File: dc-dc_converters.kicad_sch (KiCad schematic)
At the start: 62 parts, among them J3 JST_SH_1x4_SM04B-SRSS-TB-LF-SN, J4 Molex_Nano-Fit_1x2_105313-220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, U2 SIC477ED-T1-GE3, U3 AP62301WU-7, U4 AP62301WU-7

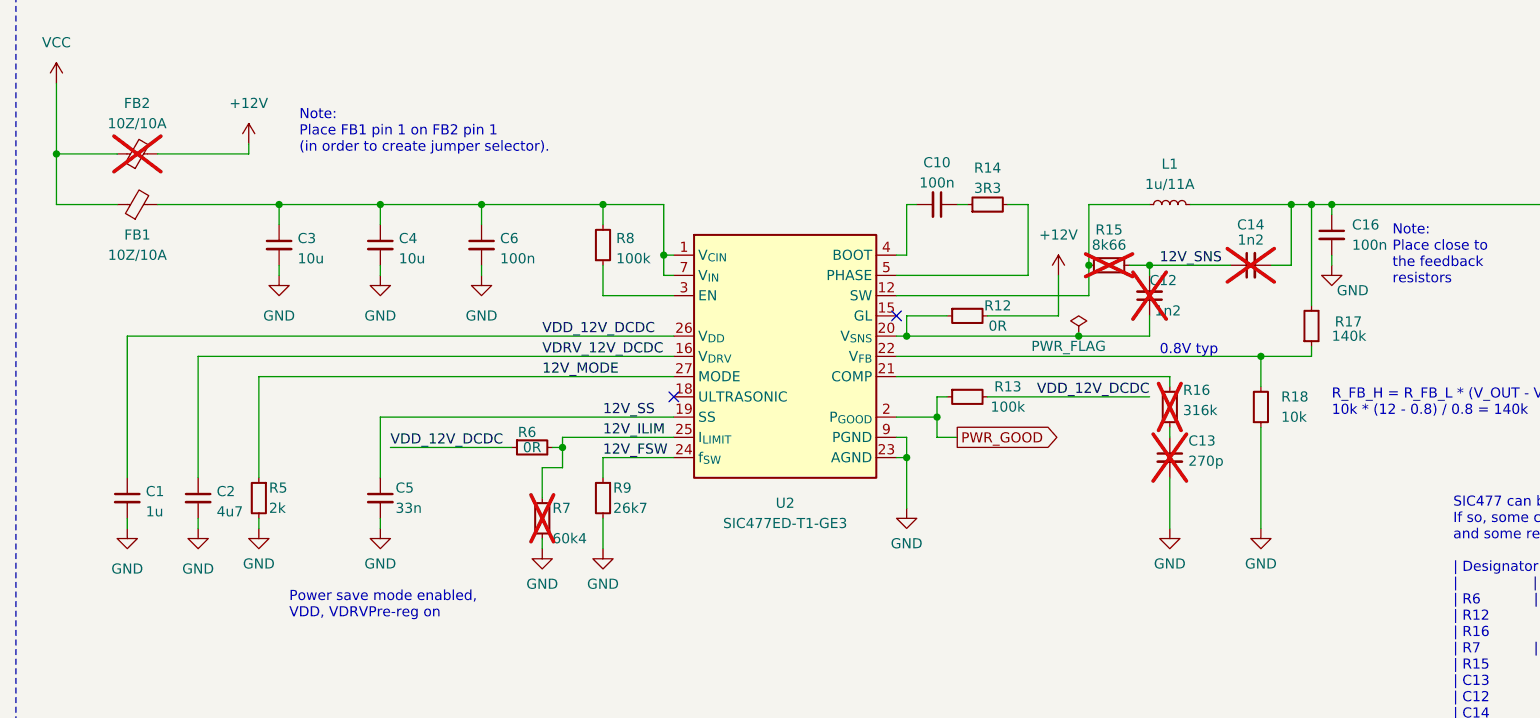
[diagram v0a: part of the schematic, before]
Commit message: [#57006] Change capacitors to higher voltage ratings
Homogenize capacitors (to not use multiple versions of the same params)
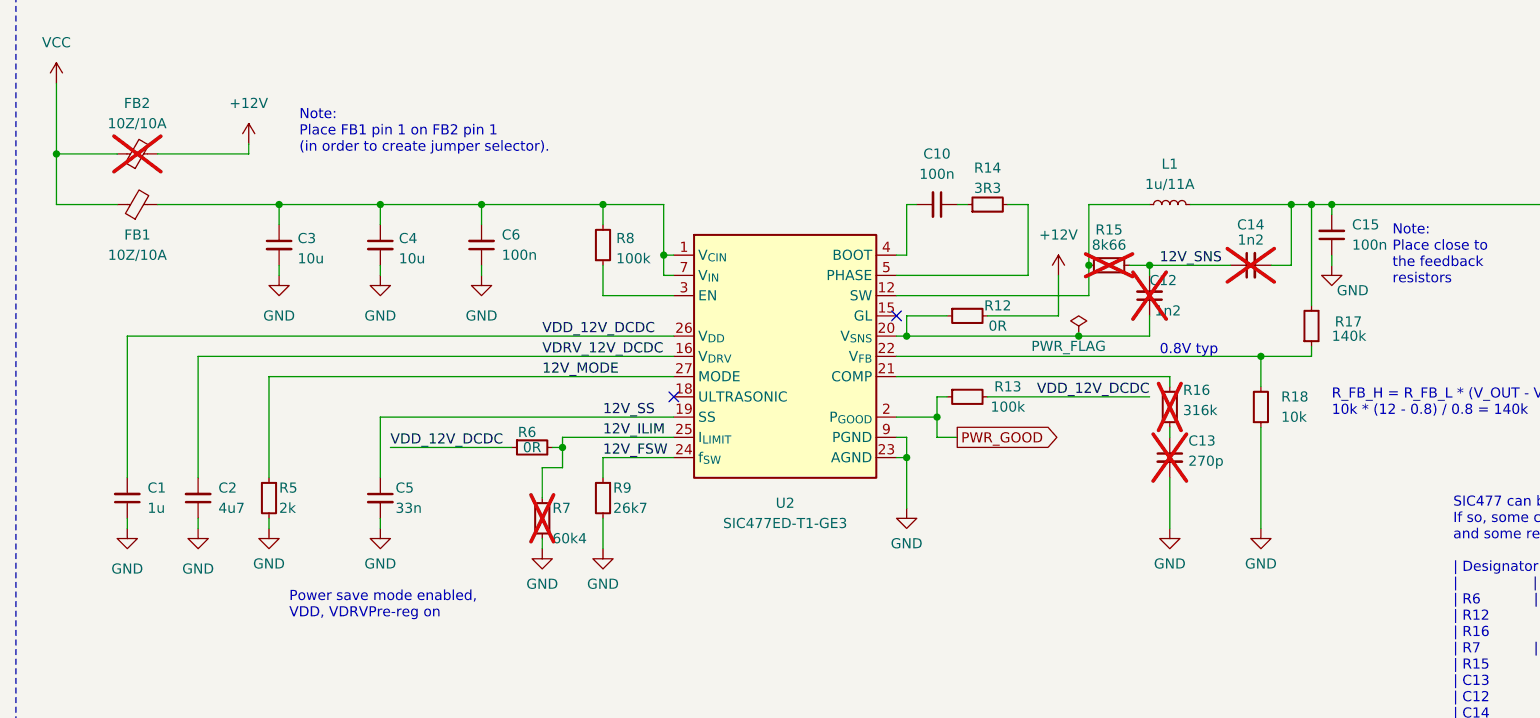
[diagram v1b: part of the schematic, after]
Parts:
- removed C1: C_1u_0402, antmicro-footprints:C_0402_1005Metric, symbol antmicroCapacitors0402:C_1u_0402
- removed C10, C16: C_100n_0402, antmicro-footprints:C_0402_1005Metric, symbol antmicroCapacitors0402:C_100n_0402
- removed C2: C_4u7_0603, antmicro-footprints:C_0603_1608Metric, symbol antmicroCapacitors0603:C_4u7_0603
- removed C6: C_100n_50V_0402, antmicro-footprints:C_0402_1005Metric, symbol antmicroCapacitorsmisc:C_100n_50V_0402
- added C1: C_1u_25V_0402, antmicro-footprints:C_0402_1005Metric, symbol antmicroCapacitors0402:C_1u_25V_0402
- added C10, C15, C6: C_100n_50V_X8L_0402, antmicro-footprints:C_0402_1005Metric, symbol antmicroCapacitors0402:C_100n_50V_X8L_0402
- added C2: C_4u7_25V_0402, antmicro-footprints:C_0402_1005Metric, symbol antmicroCapacitors0402:C_4u7_25V_0402
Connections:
- net +12V: now also C15.2
- net GND: now also C1.1, C15.1, C2.1, C6.1
- net VDD_12V_DCDC: now also C1.2
- net VDRV_12V_DCDC: now also C2.2
- net at R14.1: now also C10.1
- net at C3.1, C4.1, FB1.2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: now also C6.2
- net at U2.4 (BOOT): now also C10.2
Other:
- moved on the sheet: R5

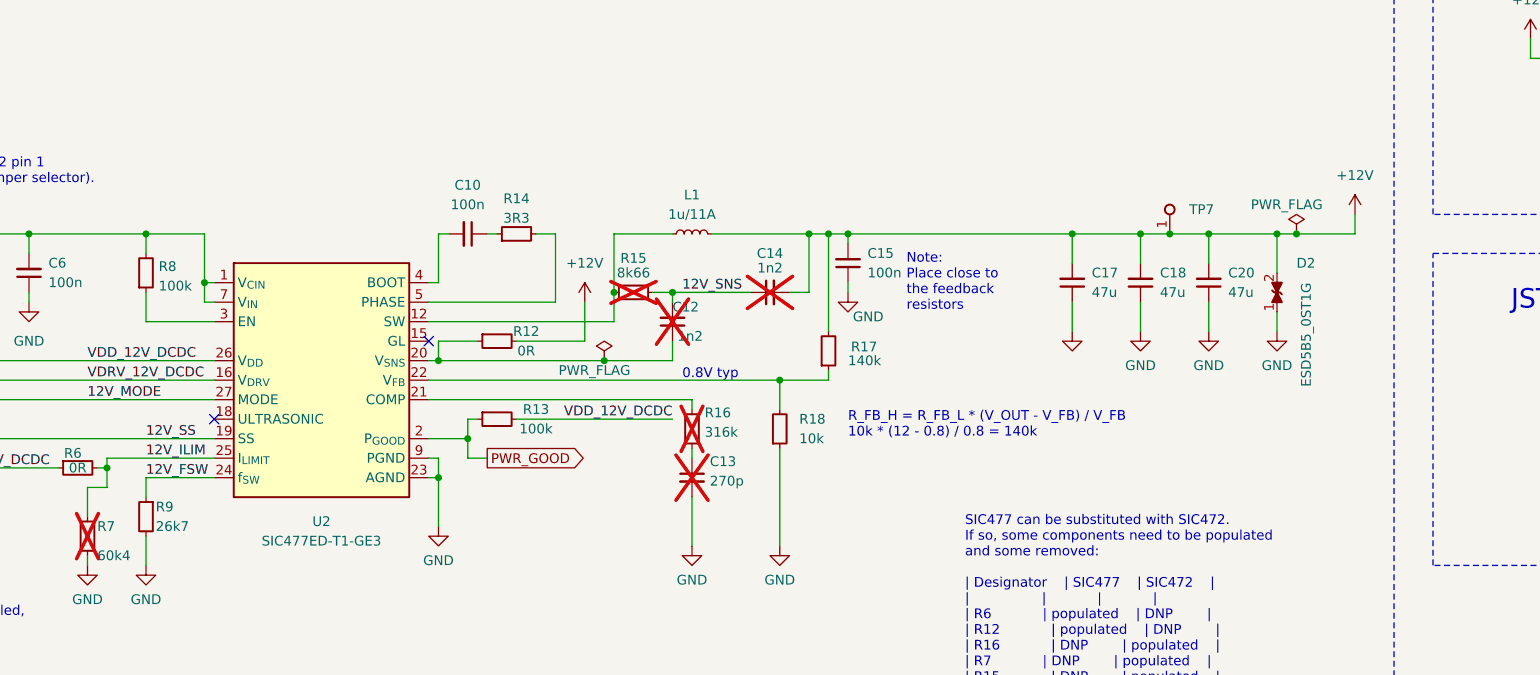
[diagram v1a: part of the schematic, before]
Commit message: [#57006] Change Rfsw to 158k
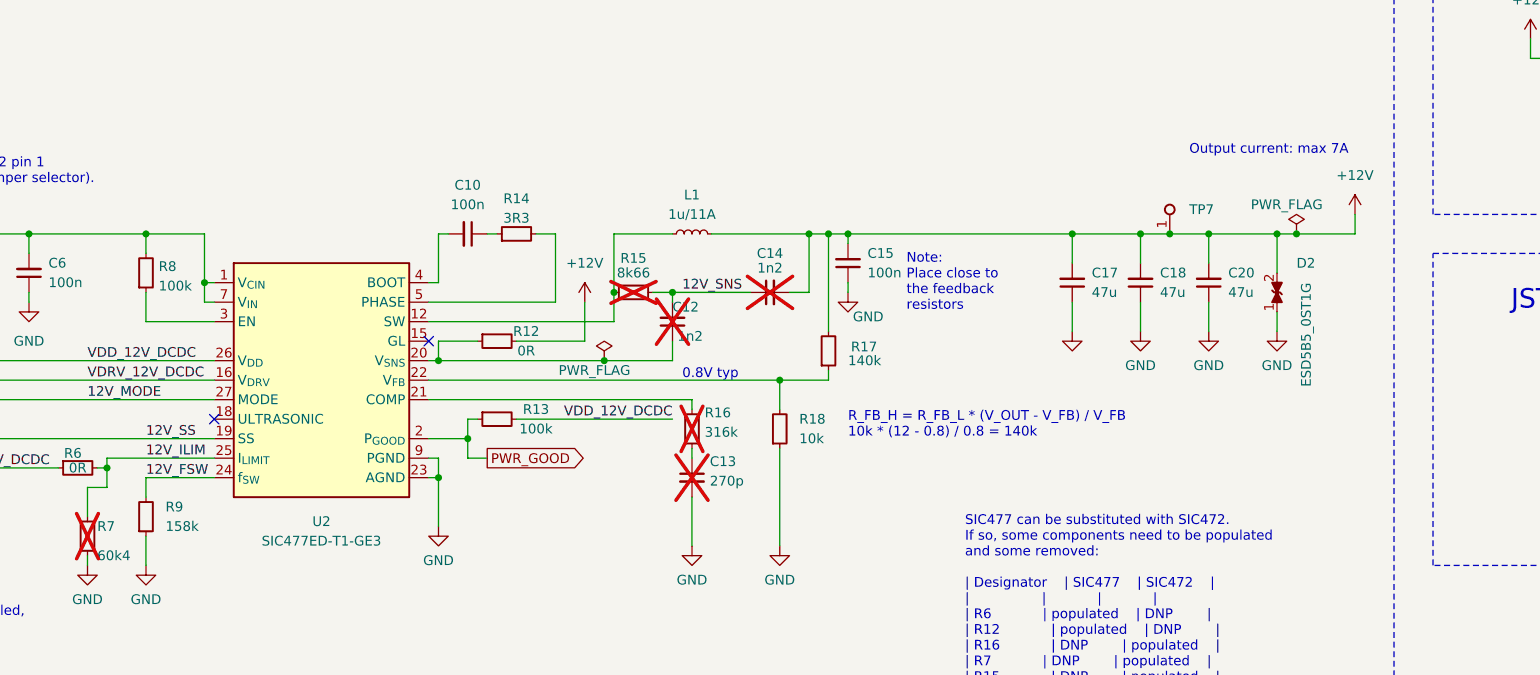
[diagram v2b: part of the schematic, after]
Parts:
- removed R9: R_26k7_0402, antmicro-footprints:R_0402_1005Metric, symbol antmicroResistors0402:R_26k7_0402
- added R9: R_158k_0402, antmicro-footprints:R_0402_1005Metric, symbol antmicroResistors0402:R_158k_0402
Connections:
- net 12V_FSW: now also R9.2
- net GND: now also R9.1
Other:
- note added: "Output current: max 7A"
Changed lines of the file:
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@@
     (effects (font (size 2.54 2.54)) (justify left bottom))
+  )
+  (text "Output current: max 7A" (at 242.57 63.5 0)
+    (effects (font (size 1.27 1.27)) (justify left bottom))
   )
   (text "+3V3 OK" (at 208.915 160.655 0)
@@
         (path "/8da33aa8-79ed-467a-95ed-bf58aa0d1db6/10c37477-f10f-4b8b-8eb5-2eccdd3a4234"
           (reference "R15") (unit 1)
-        )
-      )
-    )
-  )
-  (symbol (lib_id "antmicroResistors0402:R_26k7_0402") (at 106.68 107.95 270) (unit 1)
-    (in_bom yes) (on_board yes) (dnp no)
-    (property "Reference" "R9" (at 107.95 109.22 90)
-      (effects (font (size 1.27 1.27)) (justify left))
-    )
-    (property "Value" "R_26k7_0402" (at 102.87 107.95 0)
-      (effects (font (size 1.27 1.27)) (justify left) hide)
-    )
-    (property "Footprint" "antmicro-footprints:R_0402_1005Metric" (at 111.76 113.03 0)
-      (effects (font (size 1.27 1.27)) (justify left) hide)
-    )
-    (property "Datasheet" "https://www.bourns.com/docs/product-datasheets/cr.pdf" (at 106.68 107.95 0)
-      (effects (font (size 1.27 1.27)) (justify left) hide)
-    )
-    (property "Manufacturer" "Bourns" (at 116.84 113.03 0)
-      (effects (font (size 1.27 1.27)) (justify left) hide)
-    )
-    (property "MPN" "CR0402-FX-2672GLF" (at 114.3 113.03 0)
-      (effects (font (size 1.27 1.27)) (justify left) hide)
-    )
-    (property "Val" "26k7" (at 107.95 111.76 90)
-      (effects (font (size 1.27 1.27)) (justify left))
-    )
-    (property "License" "Apache-2.0" (at 81.28 128.27 0)
-      (effects (font (size 1.27 1.27) (thickness 0.15)) (justify left) hide)
-    )
-    (property "Author" "Antmicro" (at 78.74 128.27 0)
-      (effects (font (size 1.27 1.27) (thickness 0.15)) (justify left) hide)
-    )
-    (property "Tolerance" "1%" (at 96.52 128.27 0)
-      (effects (font (size 1.27 1.27)) (justify left) hide)
-    )
-    (pin "1")
-    (pin "2")
-    (instances
-      (project "USB-C-power-adapter"
-        (path "/8da33aa8-79ed-467a-95ed-bf58aa0d1db6/10c37477-f10f-4b8b-8eb5-2eccdd3a4234"
-          (reference "R9") (unit 1)
         )
       )
@@
         )
       )
+    )
+  )
+  (symbol (lib_id "antmicroResistors0402:R_158k_0402") (at 106.68 113.03 90) (unit 1)
+    (in_bom yes) (on_board yes) (dnp no) (fields_autoplaced)
+    (property "Reference" "R9" (at 109.22 109.22 90)
+      (effects (font (size 1.27 1.27) (thickness 0.15)) (justify right))
+    )
+    (property "Value" "R_158k_0402" (at 119.38 92.71 0)
+      (effects (font (size 1.27 1.27) (thickness 0.15)) (justify left bottom) hide)
+    )
+    (property "Footprint" "antmicro-footprints:R_0402_1005Metric" (at 121.92 92.71 0)
+      (effects (font (size 1.27 1.27) (thickness 0.15)) (justify left bottom) hide)
+    )
+    (property "Datasheet" "https://www.bourns.com/docs/product-datasheets/cr.pdf" (at 124.46 92.71 0)
+      (effects (font (size 1.27 1.27) (thickness 0.15)) (justify left bottom) hide)
+    )
+    (property "MPN" "CR0402-FX-1583GLF" (at 127 92.71 0)
+      (effects (font (size 1.27 1.27) (thickness 0.15)) (justify left bottom) hide)
+    )
+    (property "Manufacturer" "Bourns" (at 129.54 92.71 0)
+      (effects (font (size 1.27 1.27) (thickness 0.15)) (justify left bottom) hide)
+    )
+    (property "License" "Apache-2.0" (at 132.08 92.71 0)
+      (effects (font (size 1.27 1.27) (thickness 0.15)) (justify left bottom) hide)
+    )
+    (property "Author" "Antmicro" (at 134.62 92.71 0)
+      (effects (font (size 1.27 1.27) (thickness 0.15)) (justify left bottom) hide)
+    )
+    (property "Val" "158k" (at 109.22 111.76 90)
+      (effects (font (size 1.27 1.27) (thickness 0.15)) (justify right))
+    )
+    (property "Tolerance" "1%" (at 116.84 92.71 0)
+      (effects (font (size 1.27 1.27)) (justify left bottom) hide)
+    )
+    (pin "1")
+    (pin "2")
+    (instances
+      (project "USB-C-power-adapter"
+        (path "/8da33aa8-79ed-467a-95ed-bf58aa0d1db6/10c37477-f10f-4b8b-8eb5-2eccdd3a4234"
+          (reference "R9") (unit 1)
+        )
+      )

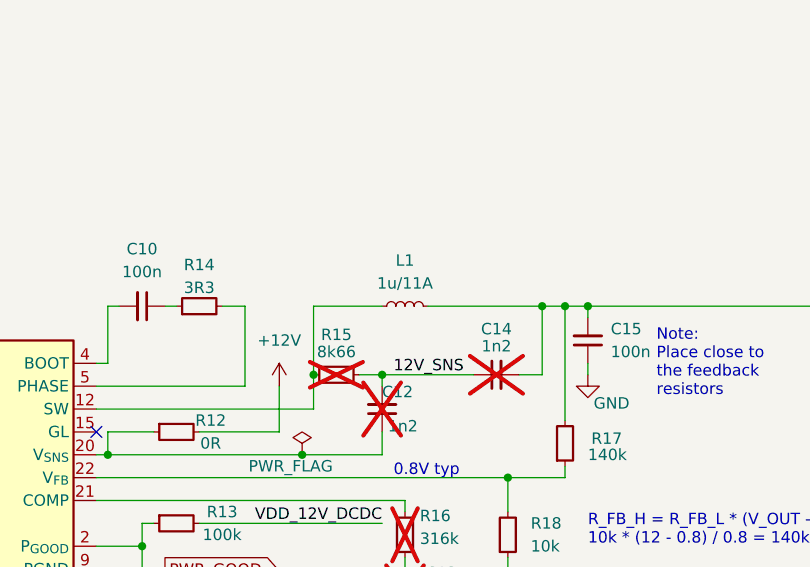
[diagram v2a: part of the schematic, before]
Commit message: [#57006] Change L1
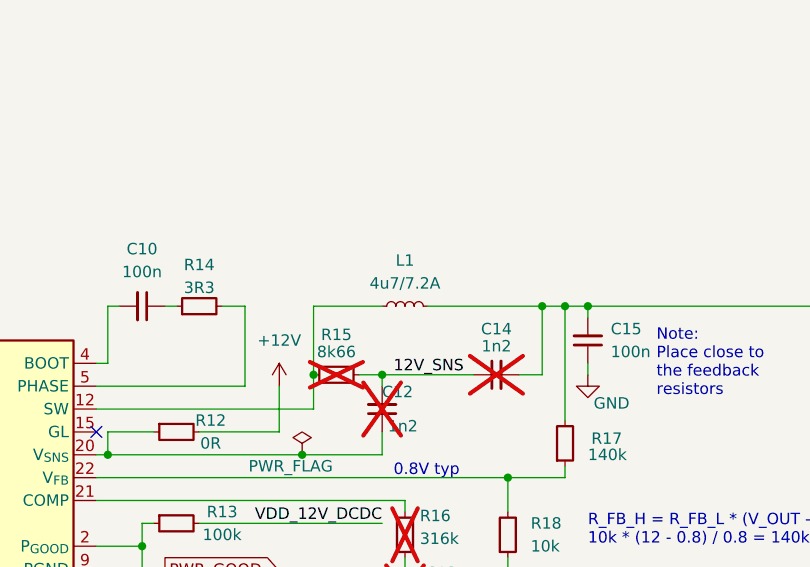
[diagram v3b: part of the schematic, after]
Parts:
- removed L1: L_1u_11A_Coilcraft-XFL4020, antmicro-footprints:L_Coilcraft-XFL4020, symbol antmicroFixedInductors:L_1u_11A_Coilcraft-XFL4020
- added L1: L_4u7_7.2A_Vishay-IHLP-3232DZ-5A, antmicro-footprints:L_Vishay-IHLP3232DZ, symbol antmicroFixedInductors:L_4u7_7.2A_Vishay-IHLP-3232DZ-5A
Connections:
- net +12V: now also L1.2
- net at R15.1, U2.12 (SW), U2.13 (SW)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: now also L1.1

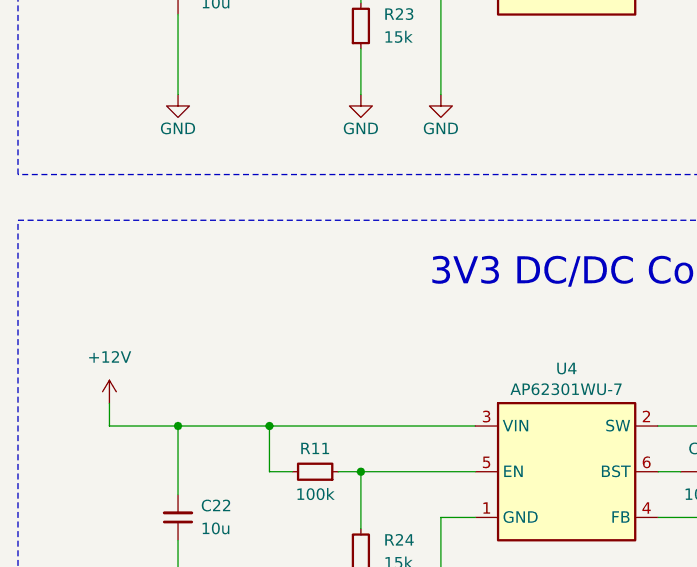
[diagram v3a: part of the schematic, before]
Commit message: [#57006] Change R3 to 0603
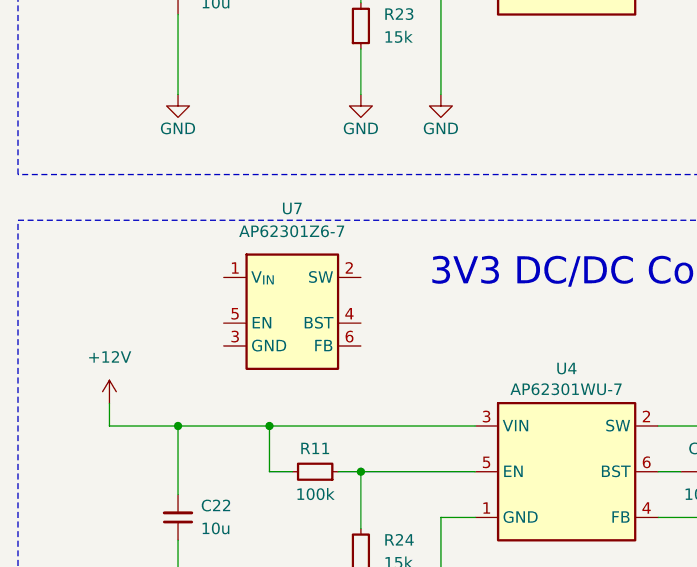
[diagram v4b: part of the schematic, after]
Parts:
- added U7: AP62301Z6-7, antmicro-footprints:SOT-563, symbol antmicroDCDCConverters:AP62301Z6-7
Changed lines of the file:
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@@
+    )
+  )
+  (symbol (lib_id "antmicroDCDCConverters:AP62301Z6-7") (at 55.88 212.09 0) (unit 1)
+    (in_bom yes) (on_board yes) (dnp no) (fields_autoplaced)
+    (property "Reference" "U7" (at 63.5 204.47 0)
+      (effects (font (size 1.27 1.27) (thickness 0.15)))
+    )
+    (property "Value" "AP62301Z6-7" (at 86.36 222.25 0)
+      (effects (font (size 1.27 1.27) (thickness 0.15)) (justify left bottom) hide)
+    )
+    (property "Footprint" "antmicro-footprints:SOT-563" (at 86.36 224.79 0)
+      (effects (font (size 1.27 1.27) (thickness 0.15)) (justify left bottom) hide)
+    )
+    (property "Datasheet" "https://www.diodes.com/assets/Datasheets/AP62300_AP62301_AP62300T.pdf" (at 86.36 227.33 0)
+      (effects (font (size 1.27 1.27) (thickness 0.15)) (justify left bottom) hide)
+    )
+    (property "MPN" "AP62301Z6-7" (at 63.5 207.01 0)
+      (effects (font (size 1.27 1.27) (thickness 0.15)))
+    )
+    (property "Manufacturer" "Diodes Incorporated" (at 86.36 229.87 0)
+      (effects (font (size 1.27 1.27) (thickness 0.15)) (justify left bottom) hide)
+    )
+    (property "Author" "Antmicro" (at 86.36 232.41 0)
+      (effects (font (size 1.27 1.27) (thickness 0.15)) (justify left bottom) hide)
+    )
+    (property "License" "Apache-2.0" (at 86.36 234.95 0)
+      (effects (font (size 1.27 1.27) (thickness 0.15)) (justify left bottom) hide)
+    )
+    (pin "2")
+    (pin "1")
+    (pin "5")
+    (pin "3")
+    (pin "6")
+    (pin "4")
+    (instances
+      (project "USB-C-power-adapter"
+        (path "/8da33aa8-79ed-467a-95ed-bf58aa0d1db6/10c37477-f10f-4b8b-8eb5-2eccdd3a4234"
+          (reference "U7") (unit 1)
+        )
+      )
     )
   )
